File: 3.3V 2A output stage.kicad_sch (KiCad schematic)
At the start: 61 parts, among them U201 MP1584EN, U202 LT3045xMSE, U203 LT3045xMSE, U204 LT3045xMSE, U205 LT3045xMSE

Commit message: correct resistor
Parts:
- R207, R208, R209, R210: value 0.2 -> 0.02
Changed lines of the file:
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@@
 			)
 		)
-		(property "Value" "0.2"
+		(property "Value" "0.02"
 			(at 359.41 161.798 90)
 			(show_name no)
@@
 			)
 		)
-		(property "Value" "0.2"
+		(property "Value" "0.02"
 			(at 359.41 47.752 90)
 			(show_name no)
@@
 			)
 		)
-		(property "Value" "0.2"
+		(property "Value" "0.02"
 			(at 359.41 123.952 90)
 			(show_name no)
@@
 			)
 		)
-		(property "Value" "0.2"
+		(property "Value" "0.02"
 			(at 359.41 85.598 90)
 			(show_name no)

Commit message: 3.3v 2a stage output mark corrected
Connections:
- net +12V renamed +3.3V
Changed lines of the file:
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@@
 			)
 		)
-		(property "Value" "+12V"
-			(at 389.382 50.8 90)
+		(property "Value" "+3.3V"
+			(at 391.414 50.8 90)
 			(show_name no)
 			(do_not_autoplace no)

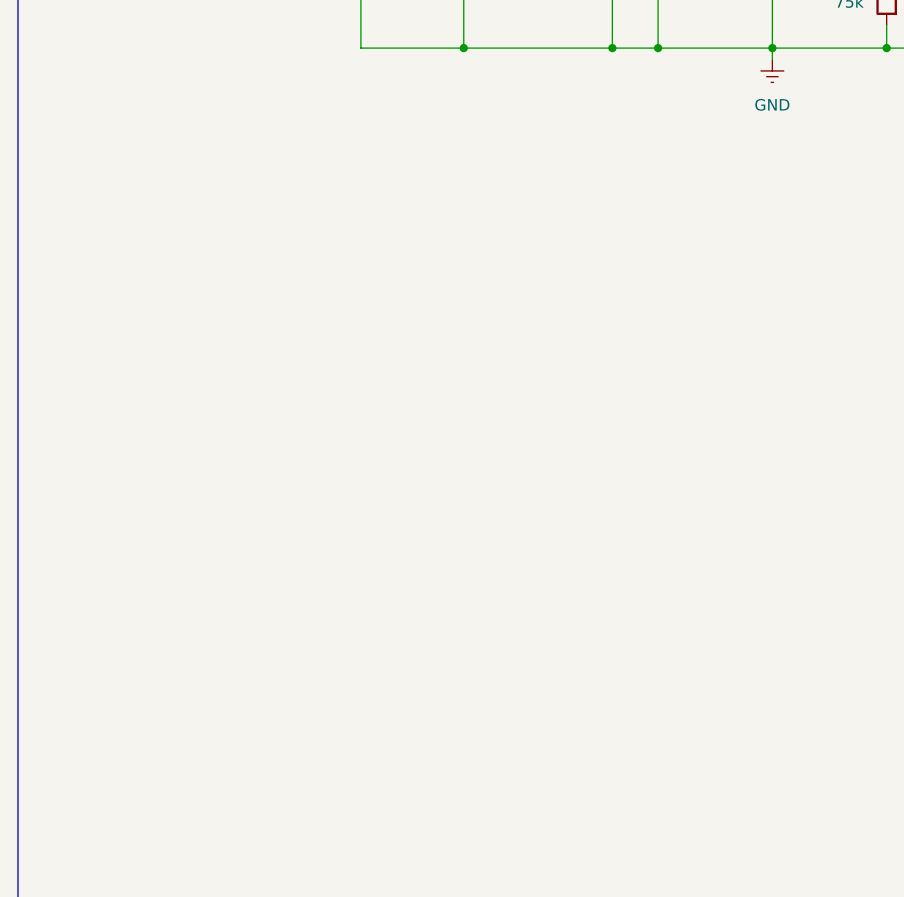
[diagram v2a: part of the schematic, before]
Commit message: Add connection testpoints and noise reduction capacitors
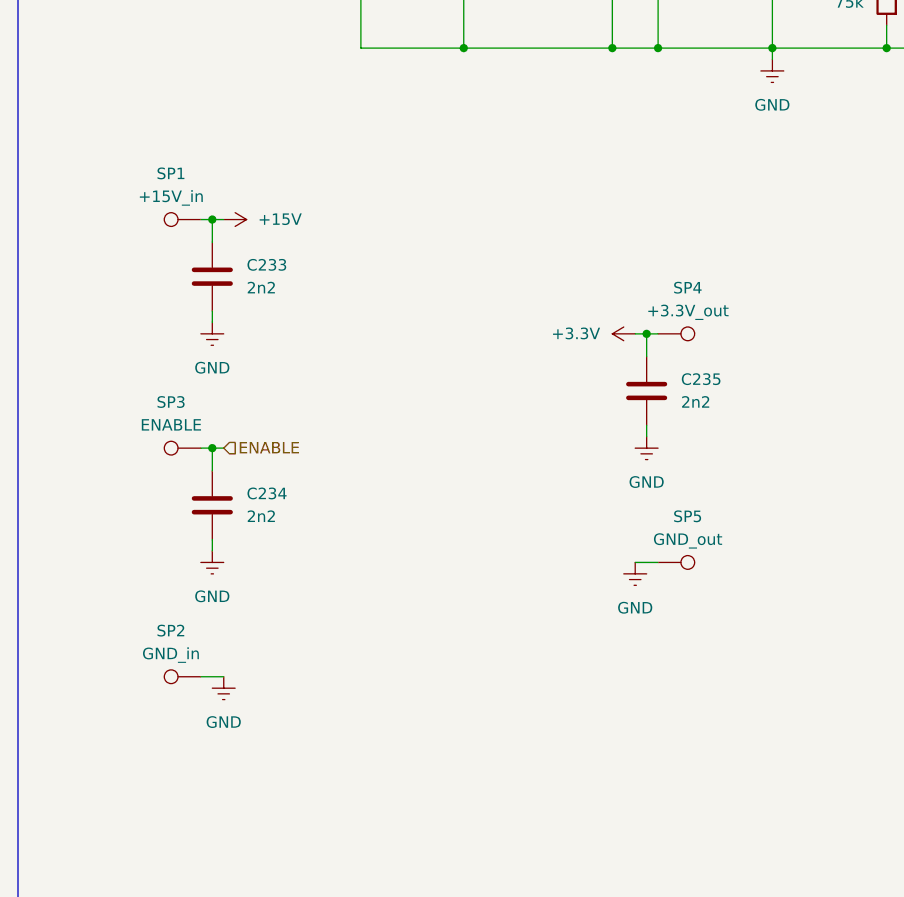
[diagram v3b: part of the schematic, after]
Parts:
- added C233, C234, C235: 2n2, symbol Device:C
- added SP1: +15V_in, symbol Connector:TestPoint
- added SP2: GND_in, symbol Connector:TestPoint
- added SP3: ENABLE, symbol Connector:TestPoint
- added SP4: +3.3V_out, symbol Connector:TestPoint
- added SP5: GND_out, symbol Connector:TestPoint
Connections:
- net +15V: now also C233.1, SP1.1
- net +3.3V: now also C235.1, SP4.1
- net ENABLE: now also C234.1, SP3.1
- net GND: now also C233.2, C234.2, C235.2, SP2.1, SP5.1

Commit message: Separate 3.3V 1A pwm output stage to another sheet
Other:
- note removed: "Плата оконечного каскада стабилизации 3.3В 2А"
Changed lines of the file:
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@@
 	(generator_version "10.0")
 	(paper "A3")
-	(rectangle
-		(start 17.78 15.24)
-		(end 402.59 250.19)
-		(stroke
-			(width 0)
-			(type default)
-		)
-		(fill
-			(type none)
-		)
-	)
 	(text "R207, R208, R209 и R210 выполнить медными проводниками\nна плате в виде дорожек определенной длины и ширины:"
 		(exclude_from_sim no)
@@
 			)
 		)
-	)
-	(text "Плата оконечного каскада стабилизации 3.3В 2А"
-		(exclude_from_sim no)
-		(at 375.92 18.034 0)
-		(effects
-			(font
-				(size 1.27 1.27)
-			)
-		)

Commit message: capacitir add
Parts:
- added C392: 33p, symbol Device:C
- C203: value 150p -> 330p
- R204: value 75k -> 100k
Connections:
- net GND: now also C392.2
- net at C203.1, U201.3 (COMP): now also C392.1
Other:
- moved on the sheet: R205
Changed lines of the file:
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@@
 	)
 	(junction
+		(at 124.46 69.85)
+		(diameter 0)
+		(color 0 0 0 0)
+	)
+	(junction
 		(at 365.76 88.9)
 		(diameter 0)
@@
 	)
 	(junction
+		(at 120.65 82.55)
+		(diameter 0)
+		(color 0 0 0 0)
+	)
+	(junction
 		(at 330.2 190.5)
 		(diameter 0)
@@
 	)
 	(junction
-		(at 119.38 69.85)
+		(at 298.45 53.34)
 		(diameter 0)
 		(color 0 0 0 0)
 	)
 	(junction
-		(at 298.45 53.34)
+		(at 290.83 190.5)
 		(diameter 0)
 		(color 0 0 0 0)
 	)
 	(junction
-		(at 290.83 190.5)
+		(at 101.6 82.55)
 		(diameter 0)
 		(color 0 0 0 0)
 	)
 	(junction
-		(at 101.6 82.55)
+		(at 114.3 60.96)
 		(diameter 0)
 		(color 0 0 0 0)
@@
 	(wire
 		(pts
+			(xy 120.65 60.96) (xy 114.3 60.96)
+		)
+		(stroke
+			(width 0)
+			(type default)
+		)
+	)
+	(wire
+		(pts
 			(xy 40.64 50.8) (xy 45.72 50.8)
 		)
@@
 	(wire
 		(pts
+			(xy 124.46 69.85) (xy 128.27 69.85)
+		)
+		(stroke
+			(width 0)
+			(type default)
+		)
+	)
+	(wire
+		(pts
 			(xy 326.39 119.38) (xy 326.39 134.62)
 		)
@@
 	(wire
 		(pts
+			(xy 120.65 63.5) (xy 120.65 60.96)
+		)
+		(stroke
+			(width 0)
+			(type default)
+		)
+	)
+	(wire
+		(pts
 			(xy 139.7 66.04) (xy 154.94 66.04)
 		)
@@
 	(wire
 		(pts
-			(xy 119.38 55.88) (xy 119.38 69.85)
+			(xy 124.46 55.88) (xy 124.46 69.85)
 		)
 		(stroke
@@
 	(wire
 		(pts
-			(xy 119.38 82.55) (xy 114.3 82.55)
+			(xy 124.46 82.55) (xy 120.65 82.55)
 		)
 		(stroke
@@
 	(wire
 		(pts
+			(xy 120.65 71.12) (xy 120.65 82.55)
+		)
+		(stroke
+			(width 0)
+			(type default)
+		)
+	)
+	(wire
+		(pts
 			(xy 279.4 165.1) (xy 279.4 167.64)
 		)
@@
 	(wire
 		(pts
-			(xy 119.38 80.01) (xy 119.38 82.55)
+			(xy 124.46 80.01) (xy 124.46 82.55)
 		)
 		(stroke
@@
 	(wire
 		(pts
-			(xy 119.38 69.85) (xy 119.38 72.39)
+			(xy 124.46 69.85) (xy 124.46 72.39)
 		)
 		(stroke
@@
 	(wire
 		(pts
-			(xy 111.76 55.88) (xy 119.38 55.88)
+			(xy 111.76 55.88) (xy 124.46 55.88)
 		)
 		(stroke
@@
 	(wire
 		(pts
-			(xy 119.38 69.85) (xy 128.27 69.85)
+			(xy 120.65 82.55) (xy 114.3 82.55)
 		)
 		(stroke
@@
 	(symbol
 		(lib_id "Device:R")
-		(at 119.38 76.2 0)
+		(at 124.46 76.2 0)
 		(unit 1)
 		(body_style 1)
@@
 		(in_pos_files yes)
 		(dnp no)
-		(fields_autoplaced yes)
 		(property "Reference" "R205"
-			(at 121.92 74.9299 0)
+			(at 127 76.708 0)
 			(show_name no)
 			(do_not_autoplace no)
@@
 		)
 		(property "Value" "40k2"
-			(at 121.92 77.4699 0)
+			(at 127 79.248 0)
 			(show_name no)
 			(do_not_autoplace no)
@@
 		)
 		(property "Footprint" ""
-			(at 117.602 76.2 90)
+			(at 122.682 76.2 90)
 			(hide yes)
 			(show_name no)
@@
 		)
 		(property "Datasheet" ""
-			(at 119.38 76.2 0)
+			(at 124.46 76.2 0)
 			(hide yes)
 			(show_name no)
@@
 		)
 		(property "Description" "Resistor"
-			(at 119.38 76.2 0)
+			(at 124.46 76.2 0)
 			(hide yes)
 			(show_name no)
@@
 		)
 		(property "MPN" "RC0805FR-0740K2L"
-			(at 119.38 76.2 0)
+			(at 124.46 76.2 0)
 			(hide yes)
 			(show_name no)
@@
 			)
 		)
-		(property "Value" "75k"
+		(property "Value" "100k"
 			(at 111.76 77.4699 0)
 			(show_name no)
@@
 			)
 		)
-		(property "Value" "150p"
+		(property "Value" "330p"
 			(at 110.49 68.5799 0)
 			(show_name no)
@@
 					(unit 1)
 				)
+			)
+		)
+	)
+	(symbol
+		(lib_id "Device:C")
+		(at 120.65 67.31 0)
+		(mirror y)
+		(unit 1)
+		(body_style 1)
+		(exclude_from_sim no)
+		(in_bom yes)
+		(on_board yes)
+		(in_pos_files yes)
+		(dnp no)
+		(property "Reference" "C392"
+			(at 120.142 70.104 0)
+			(show_name no)
+			(do_not_autoplace no)
+			(effects
+				(font
+					(size 1.27 1.27)
+				)
+				(justify left)
+			)
+		)
+		(property "Value" "33p"
+			(at 119.634 73.152 0)
+			(show_name no)
+			(do_not_autoplace no)
+			(effects
+				(font
+					(size 1.27 1.27)
+				)
+				(justify left)
+			)
+		)
+		(property "Footprint" ""
+			(at 119.6848 71.12 0)
+			(hide yes)
+			(show_name no)
+			(do_not_autoplace no)
+			(effects
+				(font
+					(size 1.27 1.27)
+				)
+			)
+		)
+		(property "Datasheet" ""
+			(at 120.65 67.31 0)
+			(hide yes)
+			(show_name no)
+			(do_not_autoplace no)
+			(effects
+				(font
+					(size 1.27 1.27)
+				)
+			)
+		)
+		(property "Description" "Unpolarized ceramic capacitor"
+			(at 120.65 67.31 0)
+			(hide yes)
+			(show_name no)
+			(do_not_autoplace no)
+			(effects
+				(font
+					(size 1.27 1.27)
+				)
+			)
+		)
+		(property "MPN" "CC0805JRNPO0BN151"
+			(at 120.65 67.31 0)
+			(hide yes)
+			(show_name no)
+			(do_not_autoplace no)
+			(effects
+				(font
+					(size 1.27 1.27)
+				)
+			)
+		)
+		(pin "1"
+		)
+		(pin "2"
+		)
+		(instances
+			(project "Low noise power supply"
+				(path "/fca69f12-2166-43a7-ac92-c50992f66d73/4931e360-a75e-47ea-922d-b3c20c53c58e"
+					(reference "C392")
+					(unit 1)
+				)
